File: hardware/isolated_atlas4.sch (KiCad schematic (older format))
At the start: 17 parts, among them J601 CONN_01X02, P6 ATLAS_ORP_PROBE, U601 ADM3260, U602 ATLAS_ORP

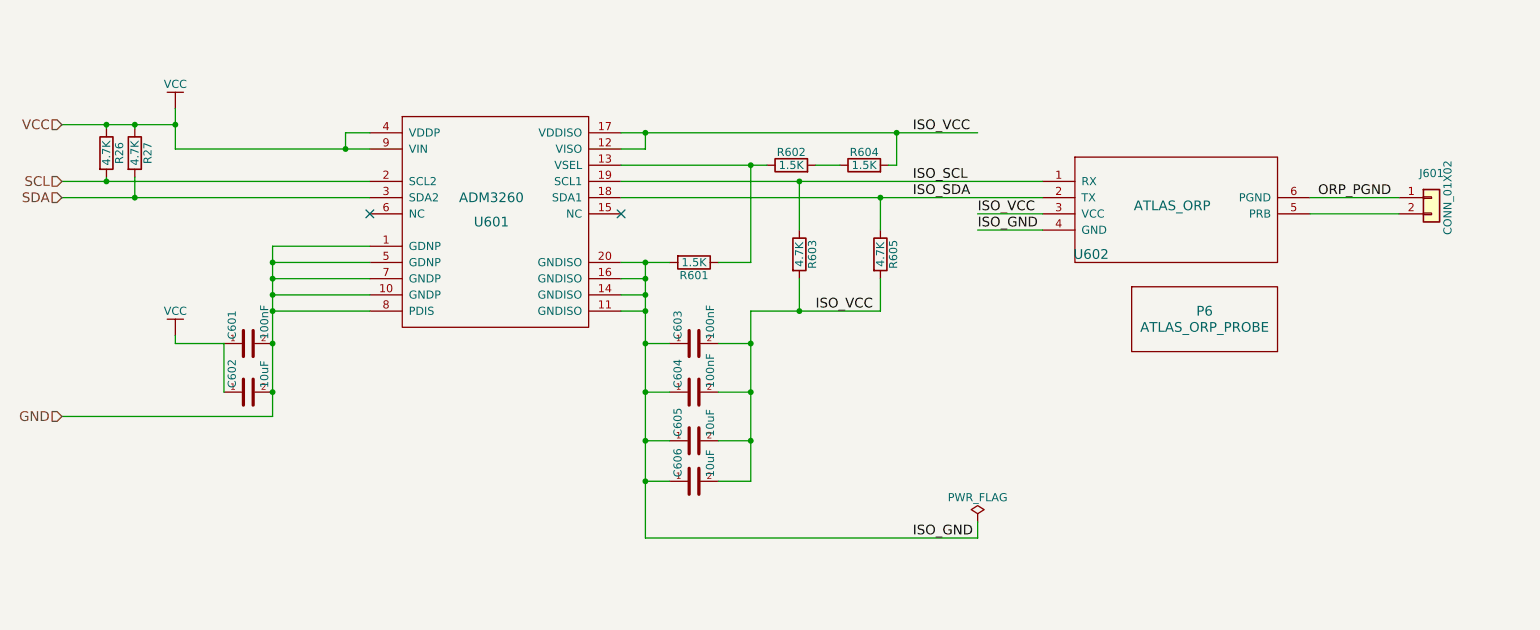
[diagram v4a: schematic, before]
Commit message: Generated panelized version of v0.11, including gerbers
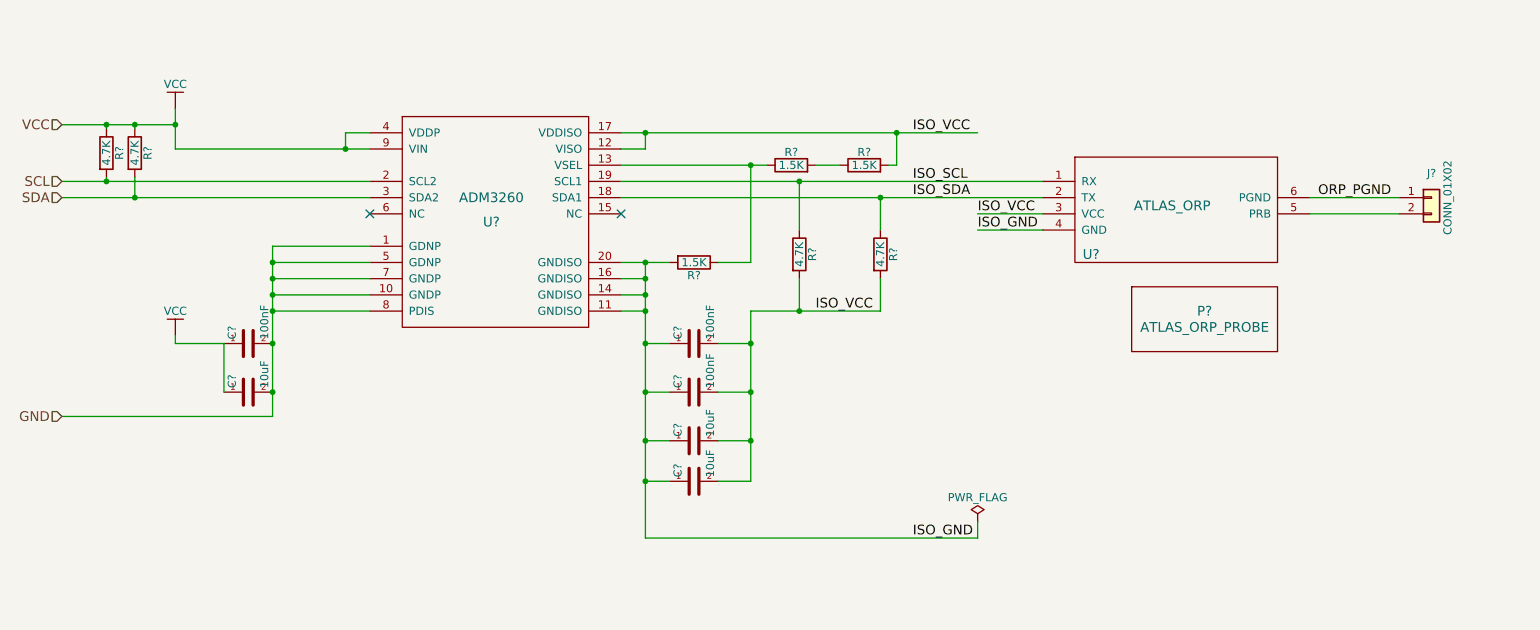
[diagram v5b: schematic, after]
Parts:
- renumbered C603 to C?, C606 to C?, C604 to C?, C605 to C?, C601 to C?, C602 to C?, J601 to J?, P6 to P?, R601 to R?, R602 to R?, R604 to R?, R603 to R?, R605 to R?, R26 to R?, R27 to R?, U602 to U?, U601 to U?
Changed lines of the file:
@@
 $EndDescr
 $Comp
-L fk-atlas-rescue:ADM3260-conservify U601
+L fk-atlas-rescue:ADM3260-conservify U?
 U 1 1 594C2CEF
 P 4400 2900
-F 0 "U601" H 4400 2750 60  0000 C CNN
+F 0 "U?" H 4400 2750 60  0000 C CNN
 F 1 "ADM3260" H 4400 2900 60  0000 C CNN
 F 2 "conservify:SSOP20-53" H 4400 2900 60  0001 C CNN
@@
 $EndComp
 $Comp
-L fk-atlas-rescue:CAPACITOR_CERAMIC-conservify C603
+L fk-atlas-rescue:CAPACITOR_CERAMIC-conservify C?
 U 1 1 5948D4BD
 P 5650 3800
-F 0 "C603" H 5675 3900 50  0000 L CNN
+F 0 "C?" H 5675 3900 50  0000 L CNN
 F 1 "100nF" H 5675 3700 50  0000 L CNN
 F 2 "conservify:CAP-0603" H 5688 3650 50  0001 C CNN
@@
 $EndComp
 $Comp
-L fk-atlas-rescue:CAPACITOR_CERAMIC-conservify C604
+L fk-atlas-rescue:CAPACITOR_CERAMIC-conservify C?
 U 1 1 594C2CFA
 P 5650 4100
-F 0 "C604" H 5675 4200 50  0000 L CNN
+F 0 "C?" H 5675 4200 50  0000 L CNN
 F 1 "100nF" H 5675 4000 50  0000 L CNN
 F 2 "conservify:CAP-0603" H 5688 3950 50  0001 C CNN
@@
 $EndComp
 $Comp
-L fk-atlas-rescue:CAPACITOR_CERAMIC-conservify C605
+L fk-atlas-rescue:CAPACITOR_CERAMIC-conservify C?
 U 1 1 594C2CFD
 P 5650 4400
-F 0 "C605" H 5675 4500 50  0000 L CNN
+F 0 "C?" H 5675 4500 50  0000 L CNN
 F 1 "10uF" H 5675 4300 50  0000 L CNN
 F 2 "conservify:CAP-0603" H 5688 4250 50  0001 C CNN
@@
 $EndComp
 $Comp
-L fk-atlas-rescue:CAPACITOR_CERAMIC-conservify C606
+L fk-atlas-rescue:CAPACITOR_CERAMIC-conservify C?
 U 1 1 5948D5D0
 P 5650 4650
-F 0 "C606" H 5675 4750 50  0000 L CNN
+F 0 "C?" H 5675 4750 50  0000 L CNN
 F 1 "10uF" H 5675 4550 50  0000 L CNN
 F 2 "conservify:CAP-0603" H 5688 4500 50  0001 C CNN
@@
 $EndComp
 $Comp
-L fk-atlas-rescue:CAPACITOR_CERAMIC-conservify C601
+L fk-atlas-rescue:CAPACITOR_CERAMIC-conservify C?
 U 1 1 594C2D05
 P 2900 3800
-F 0 "C601" H 2925 3900 50  0000 L CNN
+F 0 "C?" H 2925 3900 50  0000 L CNN
 F 1 "100nF" H 2925 3700 50  0000 L CNN
 F 2 "conservify:CAP-0603" H 2938 3650 50  0001 C CNN
@@
 $EndComp
 $Comp
-L fk-atlas-rescue:CAPACITOR_CERAMIC-conservify C602
+L fk-atlas-rescue:CAPACITOR_CERAMIC-conservify C?
 U 1 1 594C2D0A
 P 2900 4100
-F 0 "C602" H 2925 4200 50  0000 L CNN
+F 0 "C?" H 2925 4200 50  0000 L CNN
 F 1 "10uF" H 2925 4000 50  0000 L CNN
 F 2 "conservify:CAP-0603" H 2938 3950 50  0001 C CNN
@@
 $EndComp
 $Comp
-L fk-atlas-rescue:R-conservify R601
+L fk-atlas-rescue:R-conservify R?
 U 1 1 5948D6B5
 P 5650 3300
-F 0 "R601" V 5730 3300 50  0000 C CNN
+F 0 "R?" V 5730 3300 50  0000 C CNN
 F 1 "1.5K" V 5650 3300 50  0000 C CNN
 F 2 "conservify:RES-0603" V 5580 3300 50  0001 C CNN
@@
 $EndComp
 $Comp
-L fk-atlas-rescue:R-conservify R602
+L fk-atlas-rescue:R-conservify R?
 U 1 1 5948E326
 P 6250 2700
-F 0 "R602" V 6330 2700 50  0000 C CNN
+F 0 "R?" V 6330 2700 50  0000 C CNN
 F 1 "1.5K" V 6250 2700 50  0000 C CNN
 F 2 "conservify:RES-0603" V 6180 2700 50  0001 C CNN
@@
 $EndComp
 $Comp
-L fk-atlas-rescue:R-conservify R604
+L fk-atlas-rescue:R-conservify R?
 U 1 1 594C2D13
 P 6700 2700
-F 0 "R604" V 6780 2700 50  0000 C CNN
+F 0 "R?" V 6780 2700 50  0000 C CNN
 F 1 "1.5K" V 6700 2700 50  0000 C CNN
 F 2 "conservify:RES-0603" V 6630 2700 50  0001 C CNN
@@
 $EndComp
 $Comp
-L fk-atlas-rescue:R-conservify R603
+L fk-atlas-rescue:R-conservify R?
 U 1 1 594C2D18
 P 6300 3250
-F 0 "R603" V 6380 3250 50  0000 C CNN
+F 0 "R?" V 6380 3250 50  0000 C CNN
 F 1 "4.7K" V 6300 3250 50  0000 C CNN
 F 2 "conservify:RES-0603" V 6230 3250 50  0001 C CNN
@@
 $EndComp
 $Comp
-L fk-atlas-rescue:R-conservify R605
+L fk-atlas-rescue:R-conservify R?
 U 1 1 594C2D1C
 P 6800 3250
-F 0 "R605" V 6880 3250 50  0000 C CNN
+F 0 "R?" V 6880 3250 50  0000 C CNN
 F 1 "4.7K" V 6800 3250 50  0000 C CNN
 F 2 "conservify:RES-0603" V 6730 3250 50  0001 C CNN
@@
 $EndComp
 $Comp
-L fk-atlas-rescue:VCC-conservify #PWR065
+L fk-atlas-rescue:VCC-conservify #PWR?
 U 1 1 594C2D25
 P 2450 3750
-F 0 "#PWR065" H 2450 3600 50  0001 C CNN
+F 0 "#PWR?" H 2450 3600 50  0001 C CNN
 F 1 "VCC" H 2450 3900 50  0000 C CNN
 F 2 "" H 2450 3750 50  0001 C CNN
@@
 $EndComp
 $Comp
-L fk-atlas-rescue:VCC-conservify #PWR066
+L fk-atlas-rescue:VCC-conservify #PWR?
 U 1 1 594C2D27
 P 2450 2350
-F 0 "#PWR066" H 2450 2200 50  0001 C CNN
+F 0 "#PWR?" H 2450 2200 50  0001 C CNN
 F 1 "VCC" H 2450 2500 50  0000 C CNN
 F 2 "" H 2450 2350 50  0001 C CNN
@@
 $EndComp
 $Comp
-L fk-atlas-rescue:ATLAS_SENSOR-conservify U602
+L fk-atlas-rescue:ATLAS_SENSOR-conservify U?
 U 1 1 594C1D09
 P 8550 2900
-F 0 "U602" H 8100 2550 60  0000 C CNN
+F 0 "U?" H 8100 2550 60  0000 C CNN
 F 1 "ATLAS_ORP" H 8600 2850 60  0000 C CNN
 F 2 "conservify:ATLAS_SENSOR_BOARD_COMBO" H 8550 2900 60  0001 C CNN
@@
 $EndComp
 $Comp
-L fk-atlas-rescue:CONN_01x02-conservify J601
+L fk-atlas-rescue:CONN_01x02-conservify J?
 U 1 1 59A1BC7E
 P 10200 2900
-F 0 "J601" H 10200 3050 50  0000 C CNN
+F 0 "J?" H 10200 3050 50  0000 C CNN
 F 1 "CONN_01X02" V 10300 2900 50  0000 C CNN
 F 2 "conservify:BNC" H 10200 2900 50  0001 C CNN
@@
 $EndComp
 $Comp
-L fk-atlas-rescue:ATLAS_WATER_PROBE-conservify P6
+L fk-atlas-rescue:ATLAS_WATER_PROBE-conservify P?
 U 1 1 59D2AB5D
 P 8800 3600
-F 0 "P6" H 8800 3600 60  0000 C CNN
+F 0 "P?" H 8800 3600 60  0000 C CNN
 F 1 "ATLAS_ORP_PROBE" H 8800 3500 60  0000 C CNN
 F 2 "conservify:Dummy_Empty" H 8800 3600 60  0001 C CNN
@@
 $EndComp
 $Comp
-L fk-atlas-rescue:PWR_FLAG-conservify #FLG0109
+L fk-atlas-rescue:PWR_FLAG-conservify #FLG?
 U 1 1 5BCDD0A6
 P 7400 4900
-F 0 "#FLG0109" H 7400 4975 50  0001 C CNN
+F 0 "#FLG?" H 7400 4975 50  0001 C CNN
 F 1 "PWR_FLAG" H 7400 5050 50  0000 C CNN
 F 2 "" H 7400 4900 50  0001 C CNN
@@
 NoConn ~ 5200 3000
 $Comp
-L fk-atlas-rescue:R-conservify R26
+L fk-atlas-rescue:R-conservify R?
 U 1 1 5C807DB9
 P 2025 2625
-F 0 "R26" V 2105 2625 50  0000 C CNN
+F 0 "R?" V 2105 2625 50  0000 C CNN
 F 1 "4.7K" V 2025 2625 50  0000 C CNN
 F 2 "conservify:RES-0603" V 1955 2625 50  0001 C CNN
@@
 	2025 2800 3650 2800
 $Comp
-L fk-atlas-rescue:R-conservify R27
+L fk-atlas-rescue:R-conservify R?
 U 1 1 5C80B8A0
 P 2200 2625
-F 0 "R27" V 2280 2625 50  0000 C CNN
+F 0 "R?" V 2280 2625 50  0000 C CNN
 F 1 "4.7K" V 2200 2625 50  0000 C CNN
 F 2 "conservify:RES-0603" V 2130 2625 50  0001 C CNN
